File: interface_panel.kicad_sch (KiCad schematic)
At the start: 2 parts, among them J1 Conn_02x04_Odd_Even

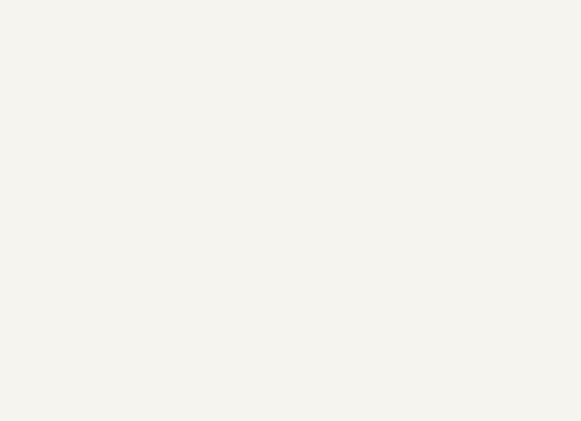
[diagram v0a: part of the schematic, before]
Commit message: ----New oled symbol added ----signal led added ----jack added
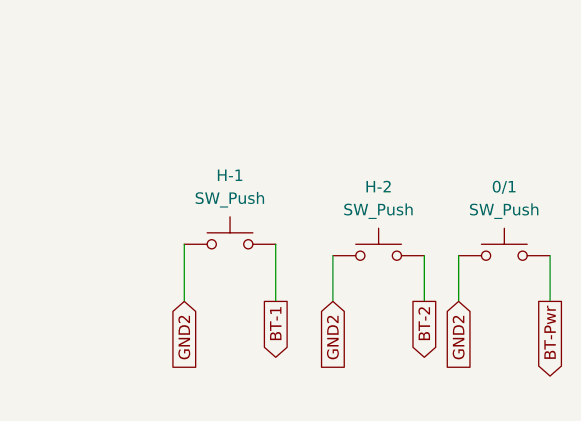
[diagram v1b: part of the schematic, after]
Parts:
- added 0/1, H-1, H-2: SW_Push, symbol Switch:SW_Push
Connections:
- new net BT-1: H-1.2
- new net BT-2: H-2.2
- new net BT-Pwr: 0/1.2
- new net GND2: 0/1.1, H-1.1, H-2.1

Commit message: same
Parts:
- added D1: LED, LED_THT:LED_D3.0mm, symbol Device:LED
- added R1: R, Resistor_THT:R_Axial_DIN0207_L6.3mm_D2.5mm_P7.62mm_Horizontal, symbol Device:R
- added oled1: ~, symbol New_Library:oled
- H-1, H-2: footprint (none) -> Button_Switch_THT:SW_PUSH_6mm
- J1: footprint (none) -> Connector_IDC:IDC-Header_2x04_P2.54mm_Vertical
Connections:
- net GND2 is gone; now on net GND: 0/1.1, H-1.1, H-2.1
- net BT-1: now also J1.3 (Pin_3)
- net BT-2: now also J1.4 (Pin_4)
- net BT-Pwr: now also J1.5 (Pin_5)
- net 5V: now reaches J1.1 (Pin_1)
- net 5V: now also oled1. (VCC)
- net GND: now reaches J1.2 (Pin_2)
- net GND: now also D1.1 (K), oled1. (VCC)
- net SCL: now reaches J1.6 (Pin_6)
- net SCL: now also oled1. (VCC)
- net SDA: now reaches J1.7 (Pin_7)
- net SDA: now also oled1. (VCC)
- net S. LED: now reaches J1.8 (Pin_8)
- net S. LED: now also R1.2
- new net: D1.2 (A), R1.1
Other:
- moved on the sheet: 0/1, H-1, H-2, J1

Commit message: PCB saved
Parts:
- 0/1: footprint (none) -> Button_Switch_THT:SW_PUSH_6mm
- oled1: footprint (none) -> oled0.9in:SSD1306-0.91-OLED-4pin-128x32
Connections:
- net 5V: now also oled1.2 (VCC); no longer oled1. (VCC)
- net BT-1: now also J1.7 (Pin_7); no longer J1.3 (Pin_3)
- net BT-2: now also J1.3 (Pin_3); no longer J1.4 (Pin_4)
- net GND: now also oled1.1 (GND); no longer oled1. (VCC)
- net S. LED: now also J1.4 (Pin_4); no longer J1.8 (Pin_8)
- net SCL: now also J1.8 (Pin_8), oled1.3 (SCL); no longer J1.6 (Pin_6), oled1. (VCC)
- net SDA: now also J1.6 (Pin_6), oled1.4 (SDA); no longer J1.7 (Pin_7), oled1. (VCC)
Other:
- note added: "COOLMAX INNOVATIONS"
- note added: "INTERFACE-PANEL"
- moved on the sheet: 0/1, D1, H-1, H-2, J1, R1

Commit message: panel_final
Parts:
- R1: footprint Resistor_THT:R_Axial_DIN0207_L6.3mm_D2.5mm_P7.62mm_Horizontal -> Resistor_THT:R_Axial_DIN0204_L3.6mm_D1.6mm_P5.08mm_Horizontal
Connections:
- net BT-1: now also J1.5 (Pin_5); no longer J1.7 (Pin_7)
- net BT-2: now also J1.7 (Pin_7); no longer J1.3 (Pin_3)
- net BT-Pwr: now also J1.3 (Pin_3); no longer J1.5 (Pin_5)
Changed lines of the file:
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@@
-		)
-	)
-	(global_label "GND"
-		(shape input)
-		(at 65.278 108.966 180)
-		(fields_autoplaced yes)
-		(effects
-			(font
-				(size 1.27 1.27)
-			)
-			(justify right)
-		)
-		(property "Intersheetrefs" "${INTERSHEET_REFS}"
-			(at 58.4223 108.966 0)
-			(effects
-				(font
-					(size 1.27 1.27)
-				)
-				(justify right)
-				(hide yes)
-			)
-		)
-	)
-	(global_label "S. LED"
-		(shape input)
-		(at 157.48 113.03 270)
-		(fields_autoplaced yes)
-		(effects
-			(font
-				(size 1.27 1.27)
-			)
-			(justify right)
-		)
-		(property "Intersheetrefs" "${INTERSHEET_REFS}"
-			(at 157.48 122.2442 90)
-			(effects
-				(font
-					(size 1.27 1.27)
-				)
-				(justify right)
-				(hide yes)
-			)
-		)
-	)
-	(global_label "GND"
-		(shape input)
-		(at 130.81 59.69 270)
-		(fields_autoplaced yes)
-		(effects
-			(font
-				(size 1.27 1.27)
-			)
-			(justify right)
-		)
-		(property "Intersheetrefs" "${INTERSHEET_REFS}"
-			(at 130.81 66.5457 90)
-			(effects
-				(font
-					(size 1.27 1.27)
-				)
-				(justify right)
-				(hide yes)
-			)
 		)
 	)
 	(global_label "BT-2"
 		(shape output)
-		(at 59.69 54.61 180)
-		(fields_autoplaced yes)
-		(effects
-			(font
-				(size 1.27 1.27)
-			)
-			(justify right)
-		)
-		(property "Intersheetrefs" "${INTERSHEET_REFS}"
-			(at 51.6853 54.61 0)
+		(at 59.69 59.69 180)
+		(fields_autoplaced yes)
+		(effects
+			(font
+				(size 1.27 1.27)
+			)
+			(justify right)
+		)
+		(property "Intersheetrefs" "${INTERSHEET_REFS}"
+			(at 51.6853 59.69 0)
 			(effects
 				(font
@@
 	(global_label "GND"
 		(shape input)
+		(at 65.278 108.966 180)
+		(fields_autoplaced yes)
+		(effects
+			(font
+				(size 1.27 1.27)
+			)
+			(justify right)
+		)
+		(property "Intersheetrefs" "${INTERSHEET_REFS}"
+			(at 58.4223 108.966 0)
+			(effects
+				(font
+					(size 1.27 1.27)
+				)
+				(justify right)
+				(hide yes)
+			)
+		)
+	)
+	(global_label "S. LED"
+		(shape input)
+		(at 157.48 113.03 270)
+		(fields_autoplaced yes)
+		(effects
+			(font
+				(size 1.27 1.27)
+			)
+			(justify right)
+		)
+		(property "Intersheetrefs" "${INTERSHEET_REFS}"
+			(at 157.48 122.2442 90)
+			(effects
+				(font
+					(size 1.27 1.27)
+				)
+				(justify right)
+				(hide yes)
+			)
+		)
+	)
+	(global_label "GND"
+		(shape input)
+		(at 130.81 59.69 270)
+		(fields_autoplaced yes)
+		(effects
+			(font
+				(size 1.27 1.27)
+			)
+			(justify right)
+		)
+		(property "Intersheetrefs" "${INTERSHEET_REFS}"
+			(at 130.81 66.5457 90)
+			(effects
+				(font
+					(size 1.27 1.27)
+				)
+				(justify right)
+				(hide yes)
+			)
+		)
+	)
+	(global_label "GND"
+		(shape input)
 		(at 161.29 59.69 270)
 		(fields_autoplaced yes)
@@
 				)
 				(justify left)
-				(hide yes)
-			)
-		)
-	)
-	(global_label "BT-Pwr"
-		(shape output)
-		(at 59.69 57.15 180)
-		(fields_autoplaced yes)
-		(effects
-			(font
-				(size 1.27 1.27)
-			)
-			(justify right)
-		)
-		(property "Intersheetrefs" "${INTERSHEET_REFS}"
-			(at 49.5081 57.15 0)
-			(effects
-				(font
-					(size 1.27 1.27)
-				)
-				(justify right)
 				(hide yes)
 			)
@@
 		)
 	)
-	(global_label "BT-1"
-		(shape output)
-		(at 59.69 59.69 180)
-		(fields_autoplaced yes)
-		(effects
-			(font
-				(size 1.27 1.27)
-			)
-			(justify right)
-		)
-		(property "Intersheetrefs" "${INTERSHEET_REFS}"
-			(at 51.6853 59.69 0)
-			(effects
-				(font
-					(size 1.27 1.27)
-				)
-				(justify right)
-				(hide yes)
-			)
-		)
-	)
 	(global_label "SCL"
 		(shape input)
@@
 		)
 	)
+	(global_label "BT-Pwr"
+		(shape output)
+		(at 59.69 54.61 180)
+		(fields_autoplaced yes)
+		(effects
+			(font
+				(size 1.27 1.27)
+			)
+			(justify right)
+		)
+		(property "Intersheetrefs" "${INTERSHEET_REFS}"
+			(at 49.5081 54.61 0)
+			(effects
+				(font
+					(size 1.27 1.27)
+				)
+				(justify right)
+				(hide yes)
+			)
+		)
+	)
 	(global_label "GND"
 		(shape input)
@@
 		(property "Intersheetrefs" "${INTERSHEET_REFS}"
 			(at 59.9947 111.506 0)
+			(effects
+				(font
+					(size 1.27 1.27)
+				)
+				(justify right)
+				(hide yes)
+			)
+		)
+	)
+	(global_label "BT-1"
+		(shape output)
+		(at 59.69 57.15 180)
+		(fields_autoplaced yes)
+		(effects
+			(font
+				(size 1.27 1.27)
+			)
+			(justify right)
+		)
+		(property "Intersheetrefs" "${INTERSHEET_REFS}"
+			(at 51.6853 57.15 0)
 			(effects
 				(font
@@
 			)
 		)
-		(property "Footprint" "Resistor_THT:R_Axial_DIN0207_L6.3mm_D2.5mm_P7.62mm_Horizontal"
+		(property "Footprint" "Resistor_THT:R_Axial_DIN0204_L3.6mm_D1.6mm_P5.08mm_Horizontal"
 			(at 155.702 107.95 90)
 			(effects
